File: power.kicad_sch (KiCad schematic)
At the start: 27 parts, among them Q1 CSD17311Q5, Q2 CSD17311Q5, U10 DS4432U+, U9 TPS40305

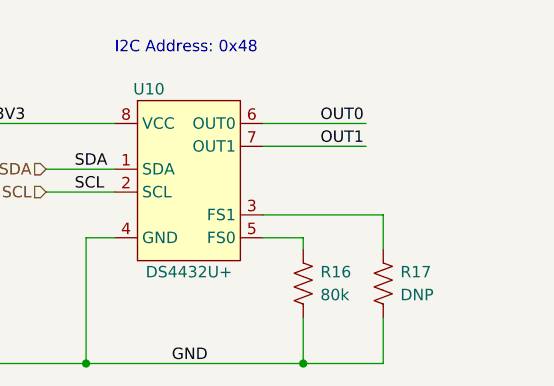
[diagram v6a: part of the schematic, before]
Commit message: added initial BOM
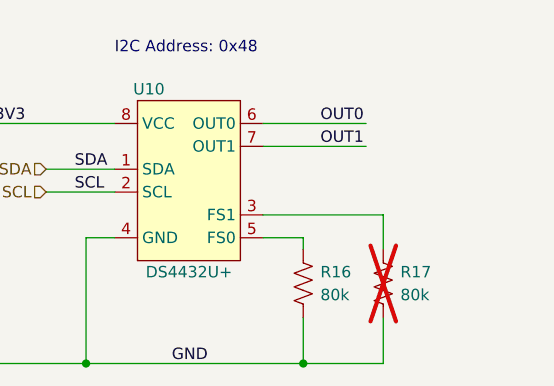
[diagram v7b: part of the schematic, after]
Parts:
- R17: value DNP -> 80k; DK (none) -> 311-80.6KLRCT-ND; PARTNO (none) -> RC0402FR-0780K6L; now not fitted
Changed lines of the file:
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@@
   )
   (symbol (lib_id "Device:R_US") (at 249.555 130.81 0) (unit 1)
-    (in_bom yes) (on_board yes) (dnp no) (fields_autoplaced)
+    (in_bom yes) (on_board yes) (dnp yes) (fields_autoplaced)
     (property "Reference" "R17" (at 251.46 129.5399 0)
       (effects (font (size 1.27 1.27)) (justify left))
     )
-    (property "Value" "DNP" (at 251.46 132.0799 0)
+    (property "Value" "80k" (at 251.46 132.0799 0)
       (effects (font (size 1.27 1.27)) (justify left))
     )
@@
       (effects (font (size 1.27 1.27)) hide)
     )
+    (property "DK" "311-80.6KLRCT-ND" (at 249.555 130.81 0)
+      (effects (font (size 1.27 1.27)) hide)
+    )
+    (property "PARTNO" "RC0402FR-0780K6L" (at 249.555 130.81 0)
+      (effects (font (size 1.27 1.27)) hide)
+    )
